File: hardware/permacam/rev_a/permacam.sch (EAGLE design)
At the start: 108 parts, among them J1 TC2030-JLINK-NL, Q1 PMDXB950UPEL, Q2 PMDXB950UPEL, Q3 PMDXB950UPEL, Q4 PMDXB950UPEL, Q5 PMDXB950UPEL, Q6 PMDXB950UPEL, U1 AB1815-T3, U10 NRF52840, U2 BQ25505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

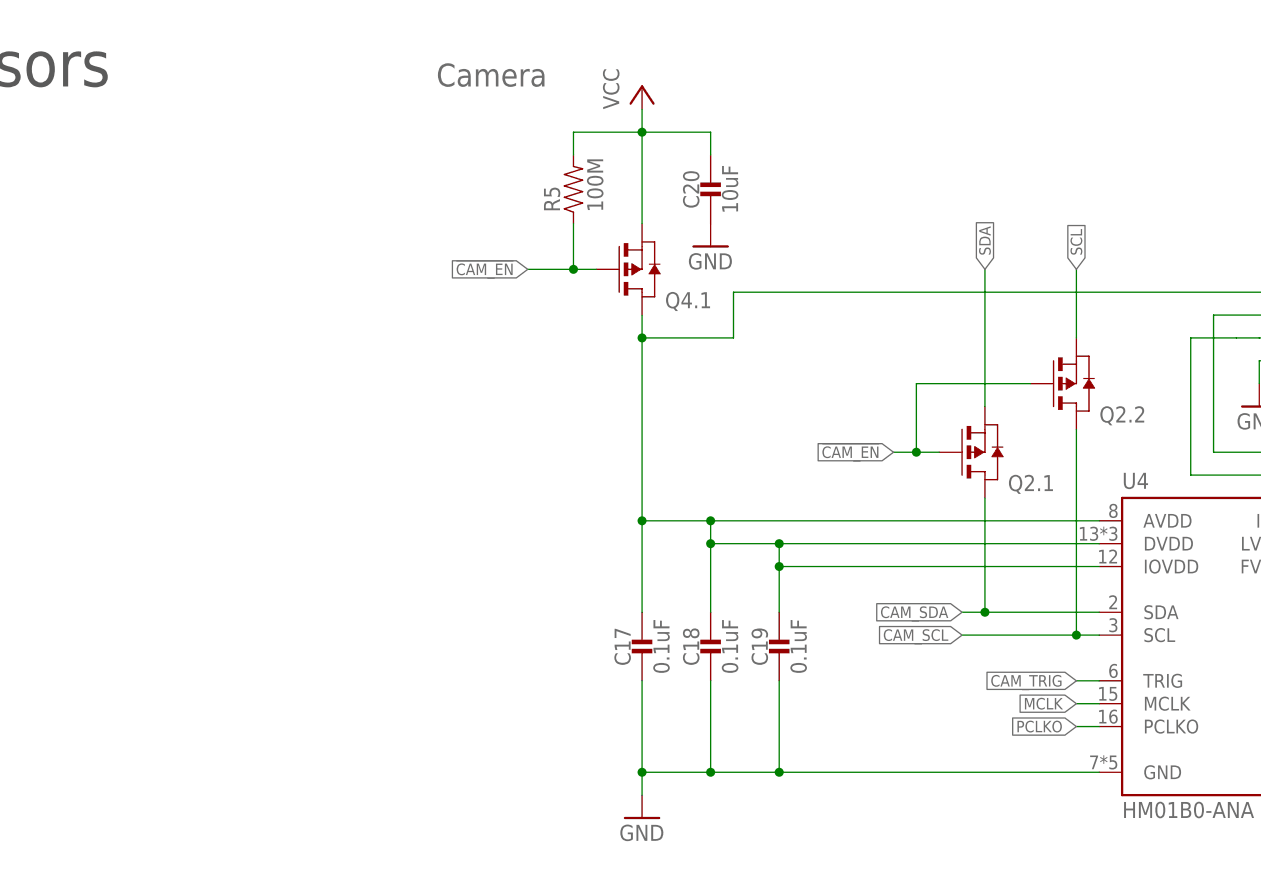
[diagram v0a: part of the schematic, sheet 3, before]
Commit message: Incorporate branden's suggestions
Add power switch, need to layout
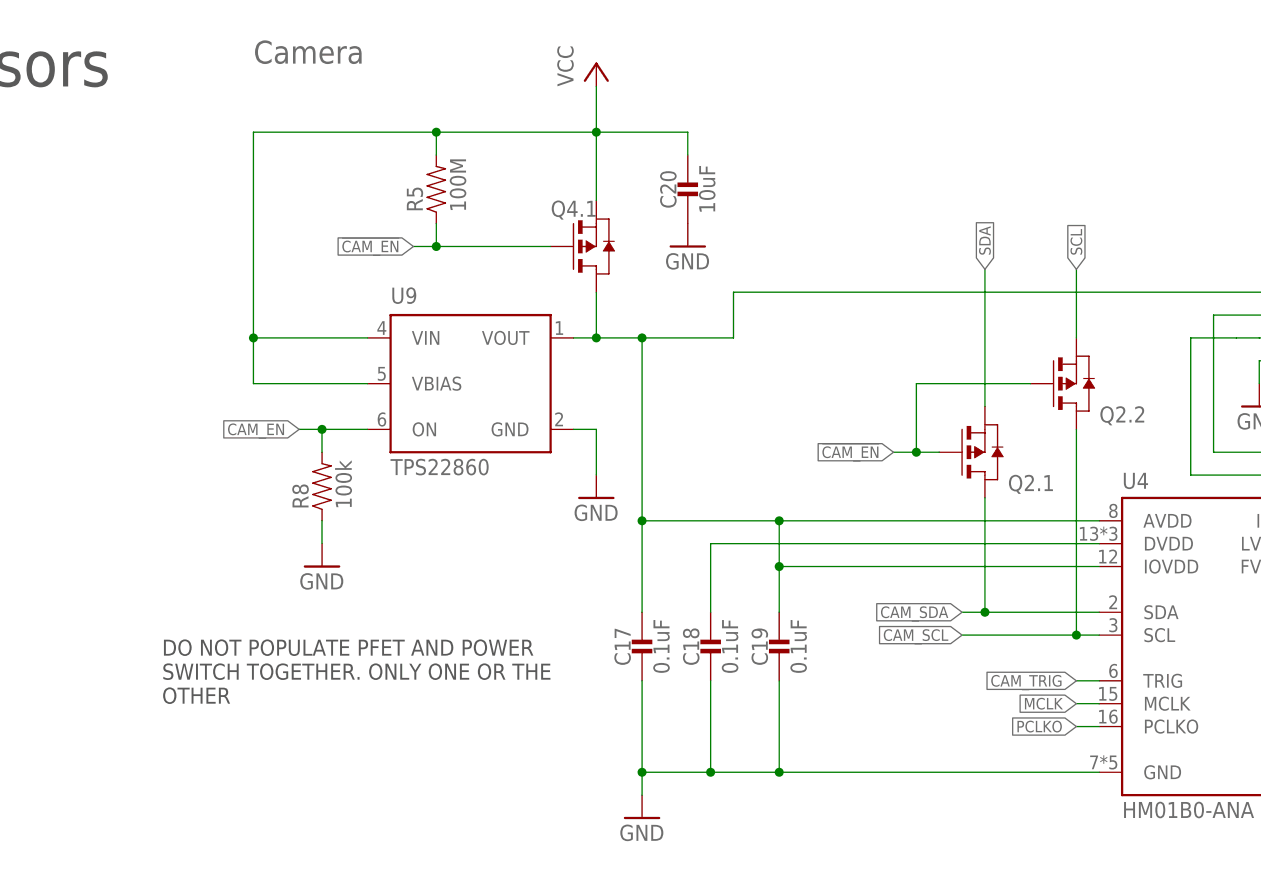
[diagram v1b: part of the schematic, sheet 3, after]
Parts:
- added R8: 100k, passives:RESISTOR0402_RES
- added U9: TPS22860, chips:TPS22860
- R13: DIGIKEY 311-80.6KHRCT-ND -> YAG3055CT-ND; MPN RC0603FR-0780K6L -> RC0402FR-07215KL
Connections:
- removed net N$16: C17.1, C18.1, C19.1, Q4.1.D, U4.AVDD, U4.DVDD, U4.IOVDD, U6.VCC
- new net CAM_EN: R8.2, U10.P0.16, U9.ON
- new net N$10: C18.1, U4.DVDD
- new net N$13: C17.1, C19.1, Q4.1.D, U4.AVDD, U4.IOVDD, U6.VCC, U9.VOUT
- net GND: now also R8.1, U9.GND
- net VCC: now also U9.VBIAS, U9.VIN
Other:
- note added: "215k results in ~2.8V output Higher than datasheet recommends Determined experimentally"
- note added: "DO NOT POPULATE PFET AND POWER SWITCH TOGETHER. ONLY ONE OR THE OTHER"
- note removed: "Only populate one MCU! Either populate the NRF52840 (Page 1) or NRF51822 (Page 2)"
- moved on the sheet: C20, Q4.1, R5

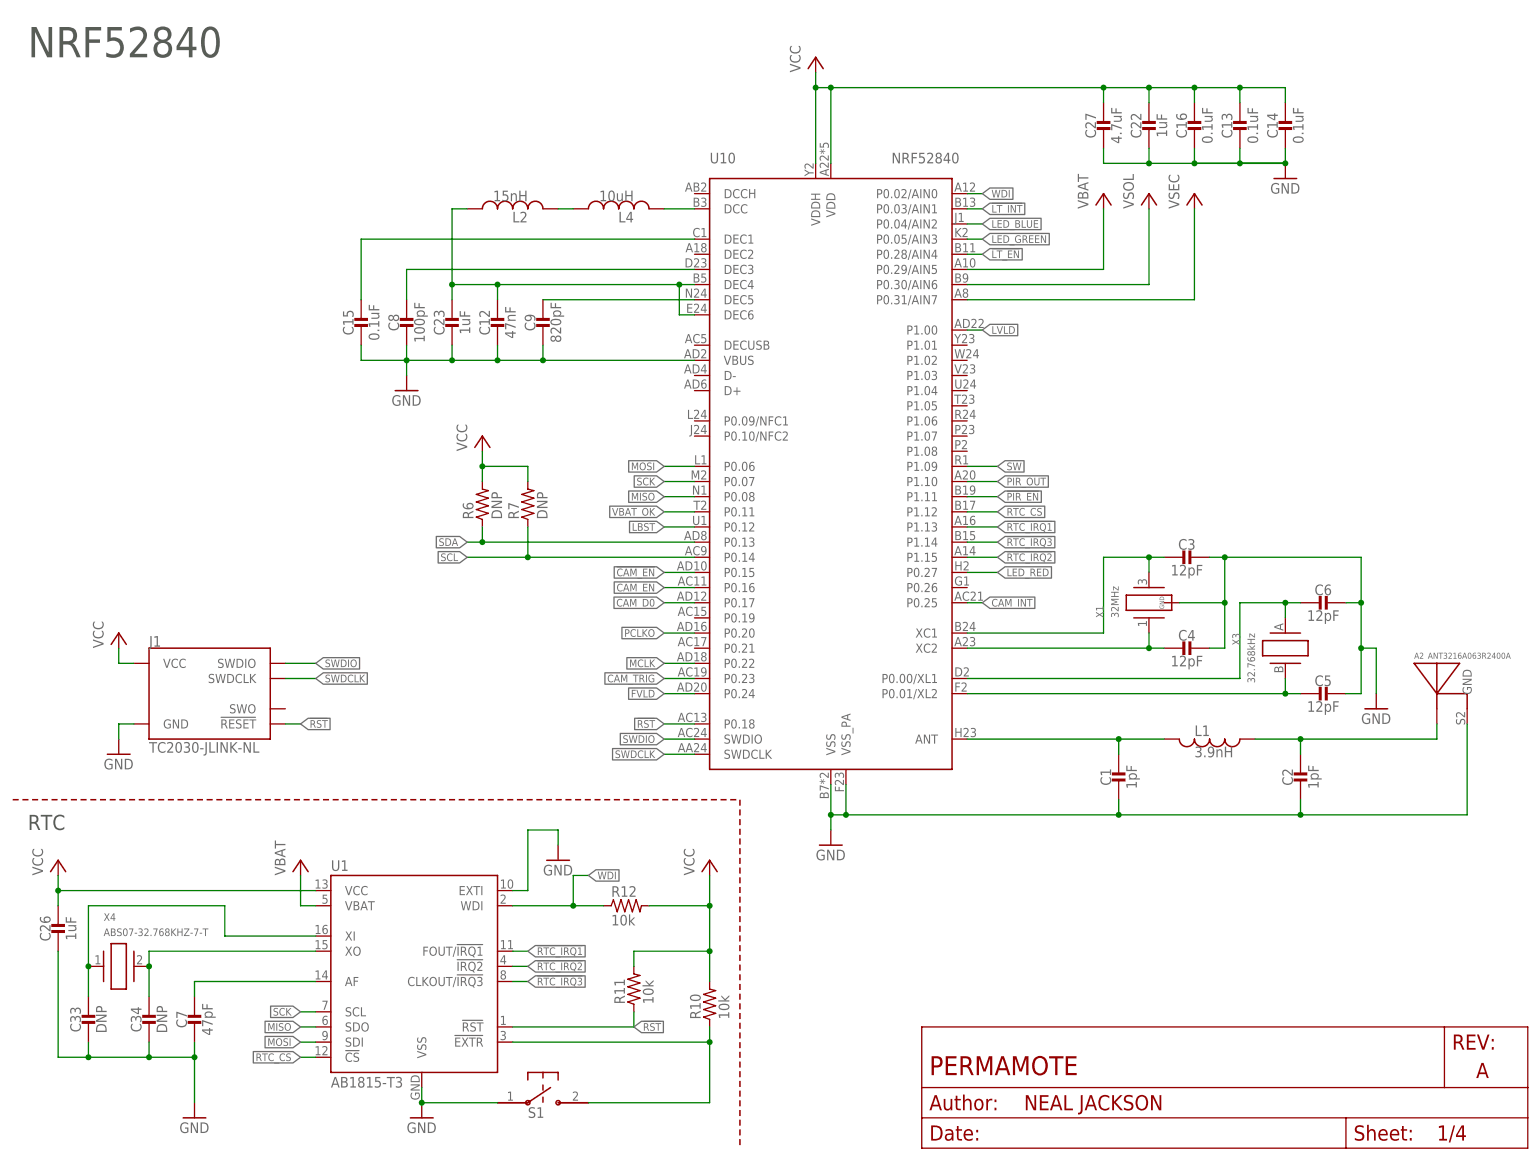
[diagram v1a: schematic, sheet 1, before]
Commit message: update part numbers
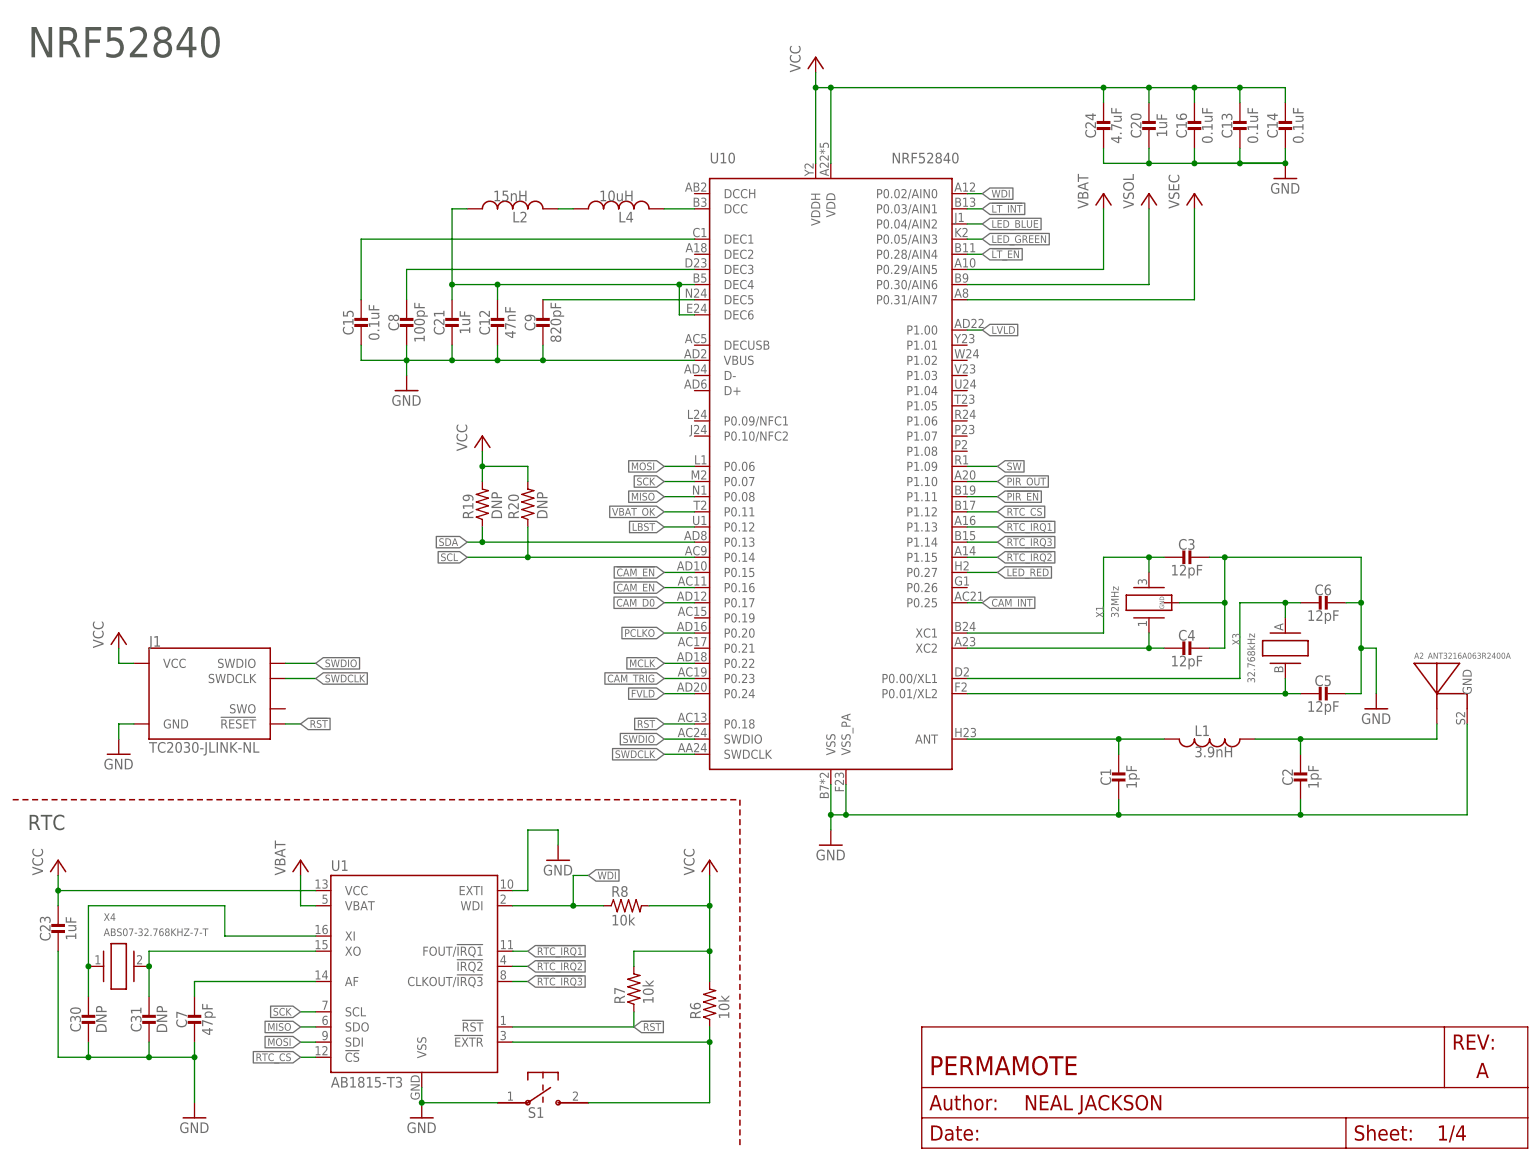
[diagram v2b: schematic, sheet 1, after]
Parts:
- removed C33, C34: DNP, passives:CAPACITOR0402_CAP
- removed R21: 9.1M, passives:RESISTOR0402_RES
- removed R27: 100M, passives:RESISTOR0402_RES
- added C21: 1uF, passives:CAPACITOR0402_CAP
- added C24: 4.7uF, passives:CAPACITOR0402_CAP
- added R19, R20: DNP, passives:RESISTOR0402_RES
- C20: value 10uF -> 1uF; device passives:CAPACITOR0603_CAP -> passives:CAPACITOR0402_CAP; DIGIKEY 490-3896-1-ND -> 490-7195-1-ND; MPN GRM188R60J106ME47D -> GRM155R70G105KA12D
- C25, C26: value 1uF -> 4.7uF; DIGIKEY 490-7195-1-ND -> 445-5947-1-ND; MPN GRM155R70G105KA12D -> C1005X5R0J475K050BC
- C27, C28, C29: value 4.7uF -> 10uF; device passives:CAPACITOR0402_CAP -> passives:CAPACITOR0603_CAP; DIGIKEY 445-5947-1-ND -> 490-3896-1-ND; MPN C1005X5R0J475K050BC -> GRM188R60J106ME47D
- C30, C31: value 10uF -> DNP; device passives:CAPACITOR0603_CAP -> passives:CAPACITOR0402_CAP; DIGIKEY 490-3896-1-ND -> (none); MPN GRM188R60J106ME47D -> (none)
- R10: value 10k -> 215k; device passives:RESISTOR0402_RES -> passives:RESISTOR0603_RES; DIGIKEY 311-10KJRCT-ND -> YAG3055CT-ND; MPN RC0402JR-0710KL -> RC0402FR-07215KL
- R11: value 10k -> 3.9M; DIGIKEY 311-10KJRCT-ND -> YAG3301CT-ND; MPN RC0402JR-0710KL -> RC0402JR-073M9L
- R12: value 10k -> 6.2M; DIGIKEY 311-10KJRCT-ND -> YAG3309CT-ND; MPN RC0402JR-0710KL -> RC0402JR-076M2L
- R13: value 215k -> 6.8M; device passives:RESISTOR0603_RES -> passives:RESISTOR0402_RES; DIGIKEY YAG3055CT-ND -> YAG3310CT-ND; MPN RC0402FR-07215KL -> RC0402JR-076M8L
- R14: value 3.9M -> 9.1M; DIGIKEY YAG3301CT-ND -> YAG3322CT-ND; MPN RC0402JR-073M9L -> RC0402JR-079M1L
- R17: value 6.2M -> 100M; DIGIKEY YAG3309CT-ND -> 541-100MAHCT-ND; MPN RC0402JR-076M2L -> HMC0402JT100M
- R18: value 6.8M -> 100M; DIGIKEY YAG3310CT-ND -> 541-100MAHCT-ND; MPN RC0402JR-076M8L -> HMC0402JT100M
- R5: value 100M -> 10k; DIGIKEY 541-100MAHCT-ND -> 311-10KJRCT-ND; MPN HMC0402JT100M -> RC0402JR-0710KL
- R6, R7: value DNP -> 10k; DIGIKEY (none) -> 311-10KJRCT-ND; MPN (none) -> RC0402JR-0710KL
- R8: value 100k -> 10k; DIGIKEY 311-100KJRCT-ND -> 311-10KJRCT-ND; MPN RC0402JR-07100KL -> RC0402JR-0710KL
- R9: value 10k -> 100k; DIGIKEY 311-10KJRCT-ND -> 311-100KJRCT-ND; MPN RC0402JR-0710KL -> RC0402JR-07100KL
- renumbered R22 to R15, R24 to R16
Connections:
- net !CAM_EN: now also R18.1; no longer R5.1
- net !LT_INT: now also R5.1; no longer R9.1
- net !PIR_EN: now also R17.1; no longer R27.1
- net !RST: now also R7.1; no longer R11.1
- net !RTC_EXTR: now also R6.1; no longer R10.1
- net CAM_EN: now also R9.2; no longer R8.2
- net GND: now also C21.2, C24.2, R10.1, R14.1, R9.1; no longer C33.2, C34.2, R18.1, R21.1, R8.1
- net N$12: now also R10.2; no longer R13.2
- net N$18: now also R11.1, R14.2; no longer R14.1, R21.2
- net N$26: now also C30.1; no longer C33.1
- net N$27: now also C31.1; no longer C34.1
- net N$3: now also C21.1; no longer C23.1
- net N$32: now also R11.2; no longer R14.2
- net N$57: now also R12.1, R13.2; no longer R17.1, R18.2
- net N$58: now also R12.2; no longer R17.2
- net SCL: now also R20.1; no longer R7.1
- net SDA: now also R19.1; no longer R6.1
- net VCC: now also C23.1, C24.1, C28.1, C29.1, R17.2, R18.2, R19.2, R20.2, R8.2; no longer C25.1, C26.1, C27.1, C31.1, R10.2, R11.2, R12.2, R27.2, R9.2
- net VOC_SAMP_VSTOR: now also C25.1; no longer C28.1
- net VSOL: now also C26.1; no longer C29.1
- net VSW: now also C27.1; no longer C30.1
- net WDI: now also R8.1; no longer R12.1
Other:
- moved on the sheet: C23, C28, R13, R14, R5, R6, R7, R9
